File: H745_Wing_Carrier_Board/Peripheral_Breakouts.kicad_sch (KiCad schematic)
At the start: 3 parts

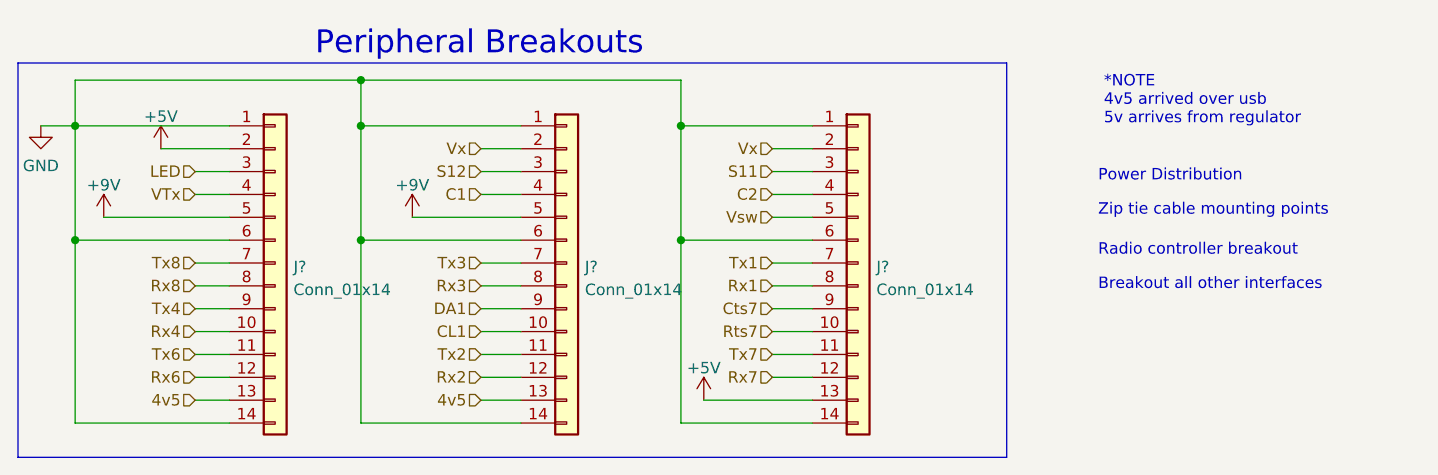
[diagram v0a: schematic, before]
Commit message: Added footprints for ux
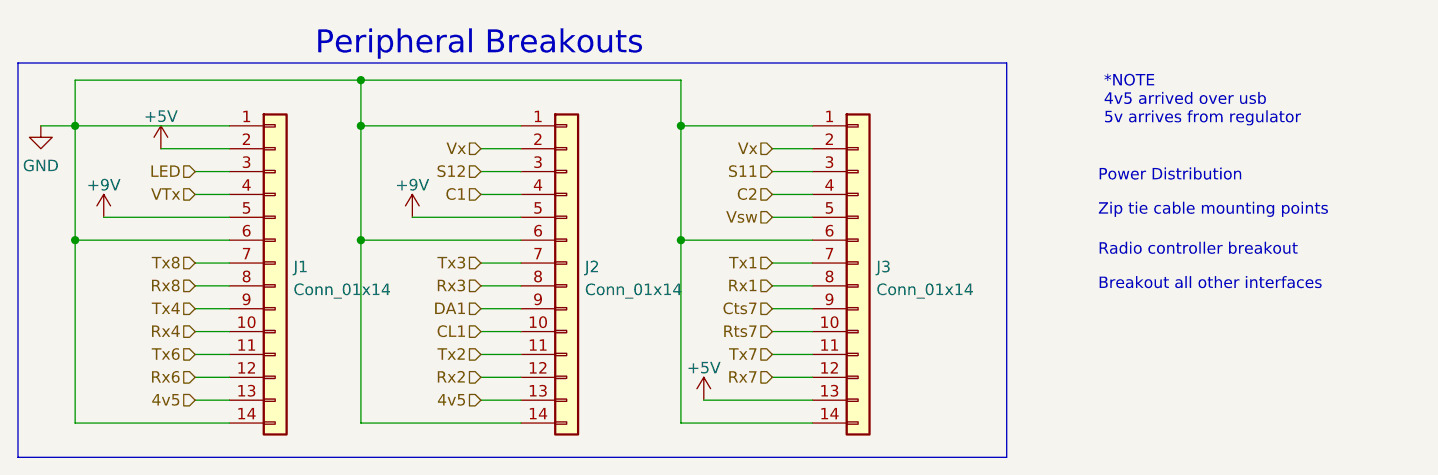
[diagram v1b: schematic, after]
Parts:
- gave numbers to parts that had none: 3
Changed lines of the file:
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@@
   (symbol (lib_id "Connector_Generic:Conn_01x14") (at 151.765 92.71 0) (unit 1)
     (in_bom yes) (on_board yes) (fields_autoplaced)
-    (property "Reference" "J?" (id 0) (at 153.797 93.1453 0)
+    (property "Reference" "J2" (id 0) (at 153.797 93.1453 0)
       (effects (font (size 1.27 1.27)) (justify left))
     )
@@
   (symbol (lib_id "Connector_Generic:Conn_01x14") (at 119.38 92.71 0) (unit 1)
     (in_bom yes) (on_board yes) (fields_autoplaced)
-    (property "Reference" "J?" (id 0) (at 121.412 93.1453 0)
+    (property "Reference" "J1" (id 0) (at 121.412 93.1453 0)
       (effects (font (size 1.27 1.27)) (justify left))
     )
@@
   (symbol (lib_id "power:+9V") (at 134.62 87.63 0) (unit 1)
     (in_bom yes) (on_board yes) (fields_autoplaced)
-    (property "Reference" "#PWR?" (id 0) (at 134.62 91.44 0)
+    (property "Reference" "#PWR0105" (id 0) (at 134.62 91.44 0)
       (effects (font (size 1.27 1.27)) hide)
     )
@@
   (symbol (lib_id "power:+5V") (at 167.005 107.95 0) (unit 1)
     (in_bom yes) (on_board yes) (fields_autoplaced)
-    (property "Reference" "#PWR?" (id 0) (at 167.005 111.76 0)
+    (property "Reference" "#PWR0104" (id 0) (at 167.005 111.76 0)
       (effects (font (size 1.27 1.27)) hide)
     )
@@
   (symbol (lib_id "power:GND") (at 93.345 77.47 0) (unit 1)
     (in_bom yes) (on_board yes) (fields_autoplaced)
-    (property "Reference" "#PWR?" (id 0) (at 93.345 83.82 0)
+    (property "Reference" "#PWR0102" (id 0) (at 93.345 83.82 0)
       (effects (font (size 1.27 1.27)) hide)
     )
@@
   (symbol (lib_id "Connector_Generic:Conn_01x14") (at 184.15 92.71 0) (unit 1)
     (in_bom yes) (on_board yes) (fields_autoplaced)
-    (property "Reference" "J?" (id 0) (at 186.182 93.1453 0)
+    (property "Reference" "J3" (id 0) (at 186.182 93.1453 0)
       (effects (font (size 1.27 1.27)) (justify left))
     )
@@
   (symbol (lib_id "power:+9V") (at 100.33 87.63 0) (unit 1)
     (in_bom yes) (on_board yes) (fields_autoplaced)
-    (property "Reference" "#PWR?" (id 0) (at 100.33 91.44 0)
+    (property "Reference" "#PWR0101" (id 0) (at 100.33 91.44 0)
       (effects (font (size 1.27 1.27)) hide)
     )
@@
   (symbol (lib_id "power:+5V") (at 106.68 80.01 0) (unit 1)
     (in_bom yes) (on_board yes) (fields_autoplaced)
-    (property "Reference" "#PWR?" (id 0) (at 106.68 83.82 0)
+    (property "Reference" "#PWR0103" (id 0) (at 106.68 83.82 0)
       (effects (font (size 1.27 1.27)) hide)
     )
